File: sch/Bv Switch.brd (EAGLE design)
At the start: 100 x 80 mm, 34 parts, among them IC1 FT232RL, IC2 7805, IC3 MEGA8-AI, IC4 74HCT595D, J2 USBHD

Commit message: Reset implementation, initial BRD
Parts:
- added C9: 100n, rcl:C1206
- added JP4: KEYPAD, pinhead:2X04
- added R8: 100, rcl:R1206
- moved JP3 290.4 mm to (47.0, 74.9)
- moved ULN1 276.1 mm to (47.0, 66.0)
- moved C8 269.2 mm to (43.2, 41.9), turned to 270 degrees
- moved IC4 261.3 mm to (47.0, 55.9), turned to 180 degrees
- moved IC3 255.1 mm to (58.4, 45.7), turned to 90 degrees
- moved JP2 231.8 mm to (77.5, 40.6), turned to 270 degrees
- moved R7 227.3 mm to (63.5, 31.8), turned to 270 degrees
- moved R6 227.2 mm to (69.8, 31.8), turned to 270 degrees
- moved R2 220.1 mm to (95.2, 73.7)
- moved C4 216.3 mm to (96.5, 21.6), turned to 270 degrees
- moved C5 213.7 mm to (82.5, 21.6), turned to 270 degrees
- moved C6 213.1 mm to (76.2, 21.6), turned to 270 degrees
- moved R4 212.7 mm to (91.4, 48.3)
- moved C7 211.1 mm to (21.6, 33.0), turned to 270 degrees
- moved +5V 209.9 mm to (88.9, 53.3)
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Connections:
- removed net N$9: IC3.29, JP2.5, R5.1
- new net N$36: C9.2, IC1.2
- new net N$37: IC1.3, R8.1
- new net RESET: C9.1, IC3.29, JP2.5, R5.1, R8.2
- new net SCL: IC3.28, JP4.5
- new net SDA: IC3.27, JP4.3
- net +5V: now also JP4.1, JP4.2, JP4.4
- net GND: now also JP4.6, JP4.7, JP4.8

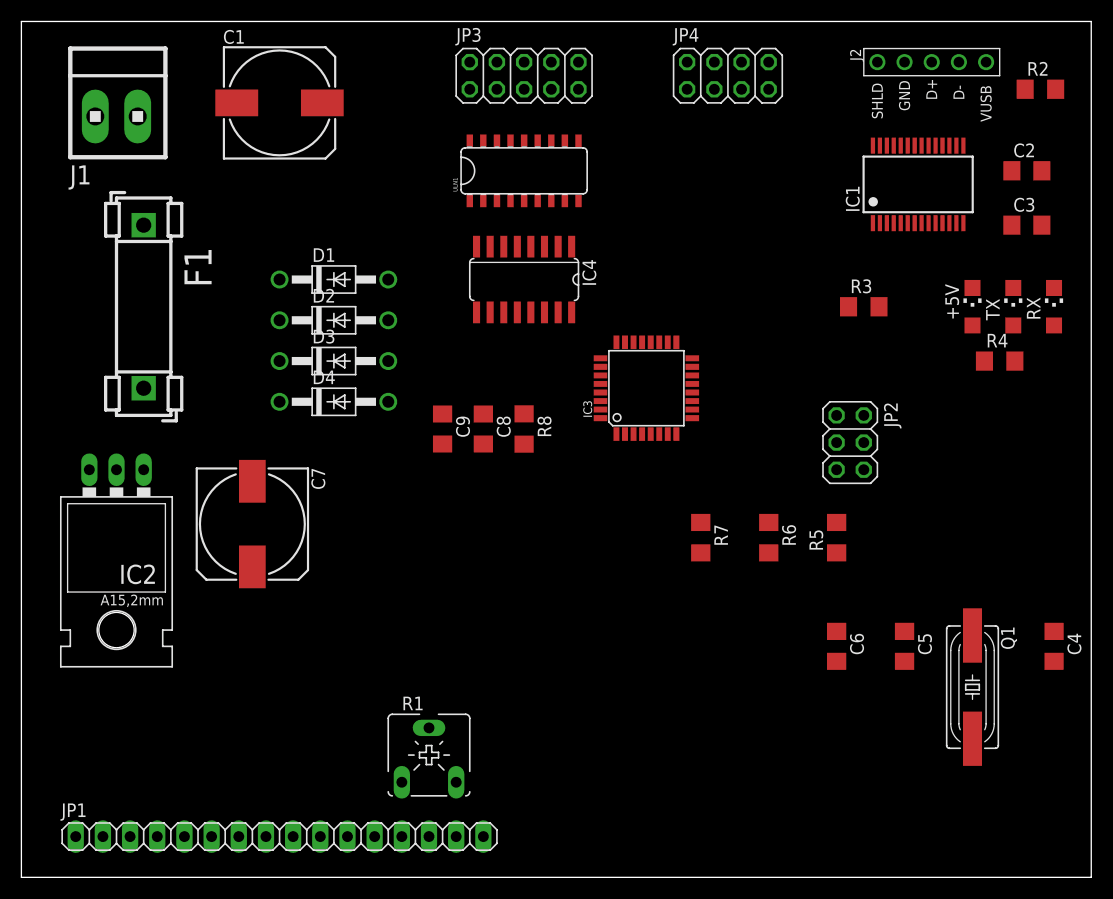
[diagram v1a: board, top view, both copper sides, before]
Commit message: Added Bv-Remote, BRD and 3d generation
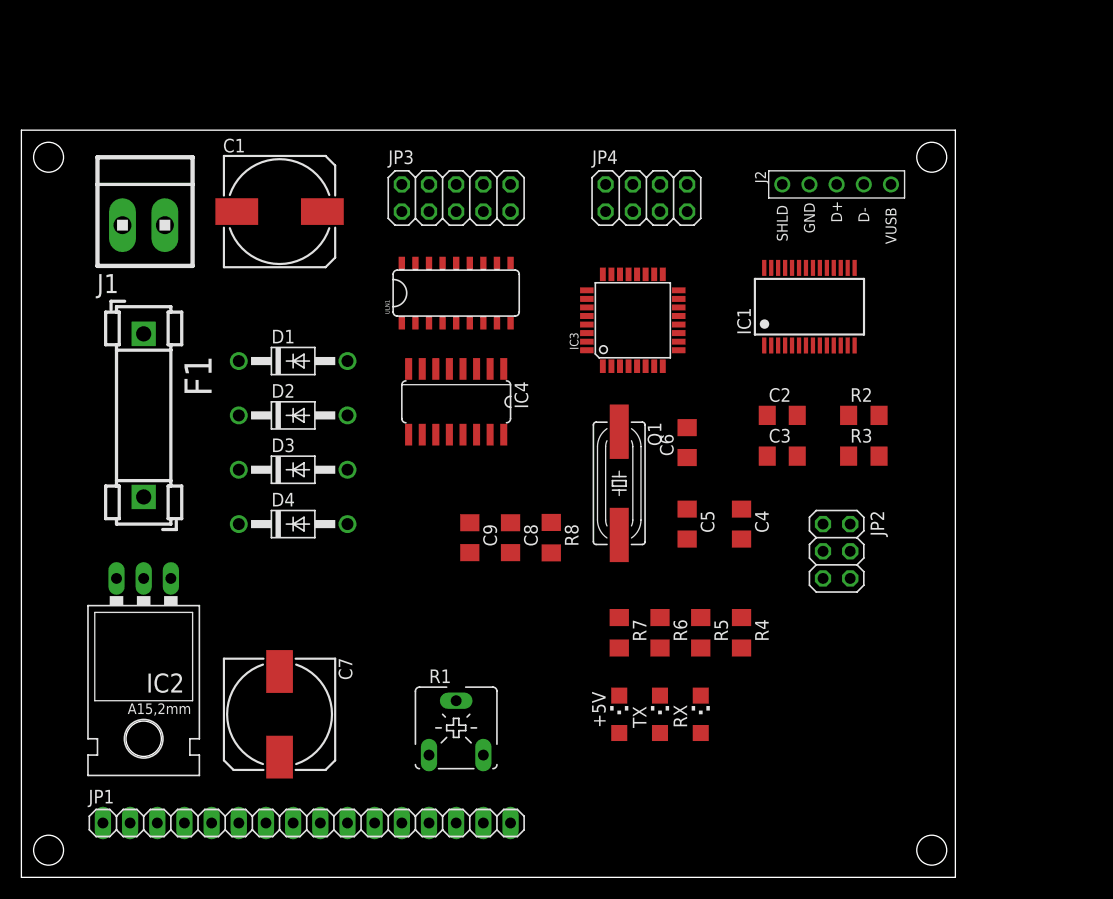
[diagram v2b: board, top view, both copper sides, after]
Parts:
- moved +5V 50.4 mm to (55.9, 15.2)
- moved RX 50.4 mm to (63.5, 15.2)
- moved TX 50.4 mm to (59.7, 15.2)
- moved Q1 38.1 mm to (55.9, 36.8)
- moved R4 35.0 mm to (67.3, 22.9), turned to 270 degrees
- moved R2 34.7 mm to (78.7, 43.2)
- moved C2 32.3 mm to (71.1, 43.2)
- moved C3 31.4 mm to (71.1, 39.4)
- moved C4 31.4 mm to (67.3, 33.0)
- moved C6 23.6 mm to (62.2, 40.6), turned to 90 degrees
- moved C5 23.3 mm to (62.2, 33.0)
- moved C7 18.0 mm to (24.1, 15.2)
- moved R5 15.5 mm to (63.5, 22.9), turned to 270 degrees
- moved IC1 15.3 mm to (73.7, 53.3)
- moved J2 14.5 mm to (81.3, 64.8)
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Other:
- board size 100 x 80 mm -> 87.3 x 69.8 mm
